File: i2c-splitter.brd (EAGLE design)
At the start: 23.5 x 23.5 mm, 5 parts

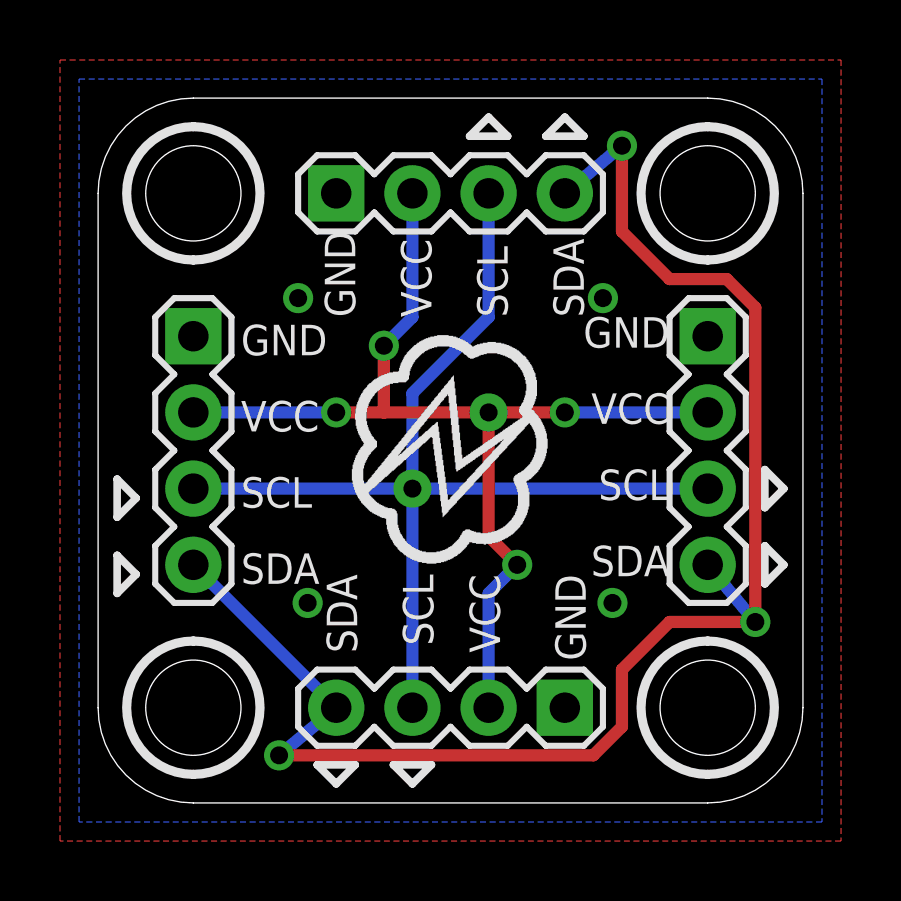
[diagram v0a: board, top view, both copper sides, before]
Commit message: reversed headers
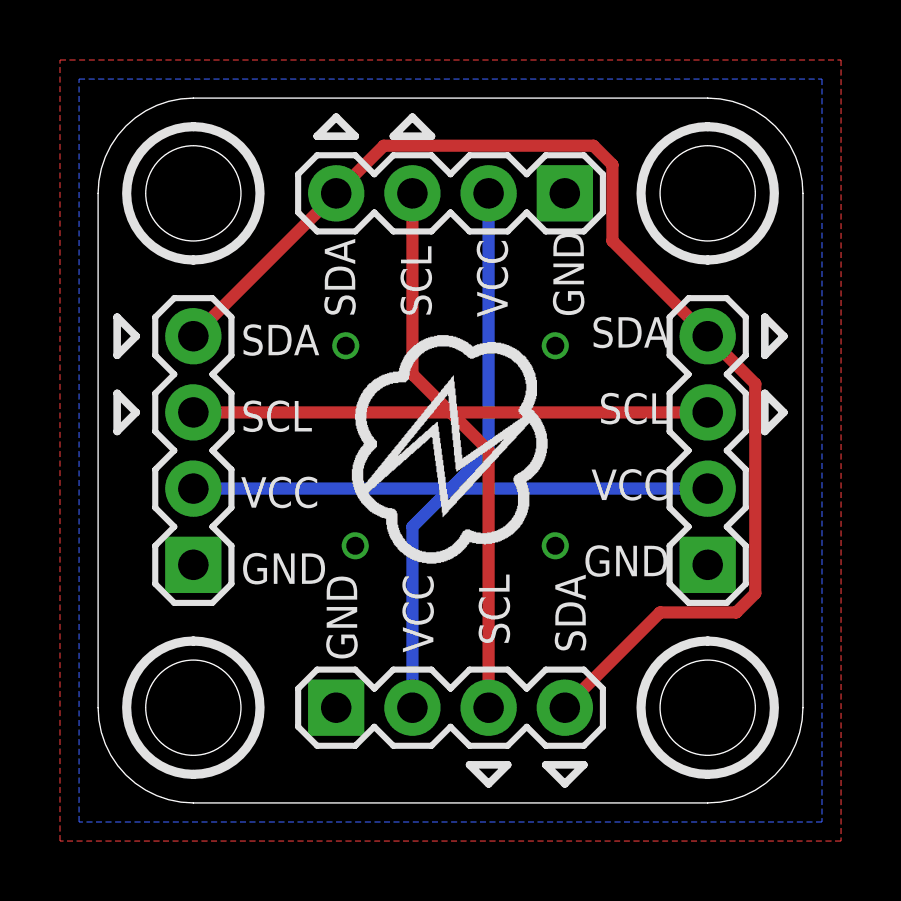
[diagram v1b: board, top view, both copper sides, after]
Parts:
- moved JP1 7.62 mm to (3.17, 7.94), turned to 90 degrees
- moved JP2 7.62 mm to (15.6, 20.3), turned to 180 degrees
- moved JP3 7.62 mm to (20.3, 7.94), turned to 90 degrees
- moved JP4 7.62 mm to (7.94, 3.17), turned to 0 degrees
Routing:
- net SDA: track 51.8 -> 41.1 mm, vias 3 -> 0
- net VCC: track 35.5 -> 35.3 mm, vias 5 -> 0
- net SCL: vias 1 -> 0
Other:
- board text added: "I2C Splitter IX01"
- board text removed: "I2C Splitter IS01"

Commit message: optional bypass capacitor
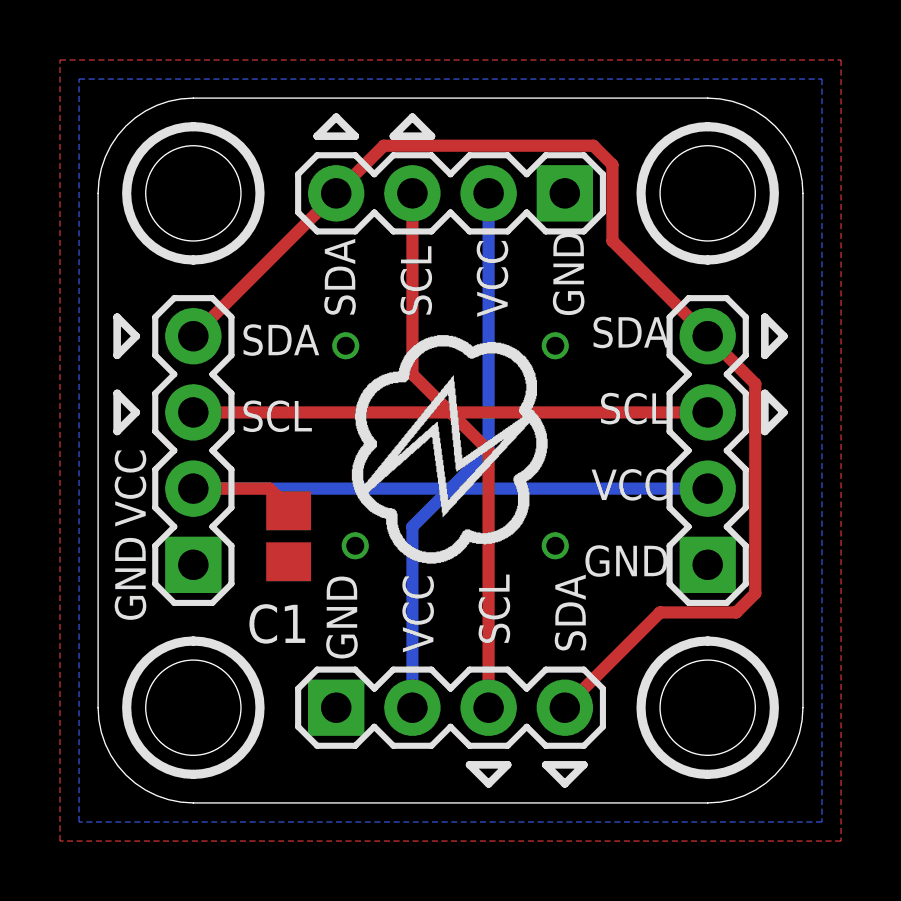
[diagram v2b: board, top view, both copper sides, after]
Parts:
- added C1: 100 nF, resistor:C0805
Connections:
- net GND: now also C1.2
- net VCC: now also C1.1
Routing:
- net VCC: track 35.3 -> 39.0 mm
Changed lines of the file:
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@@
 <layer number="20" name="Dimension" color="15" fill="1" visible="yes" active="yes"/>
 <layer number="21" name="tPlace" color="14" fill="1" visible="yes" active="yes"/>
-<layer number="22" name="bPlace" color="13" fill="1" visible="no" active="yes"/>
+<layer number="22" name="bPlace" color="13" fill="1" visible="yes" active="yes"/>
 <layer number="23" name="tOrigins" color="15" fill="1" visible="yes" active="yes"/>
 <layer number="24" name="bOrigins" color="15" fill="1" visible="yes" active="yes"/>
@@
 <text x="4.7625" y="14.9225" size="1.016" layer="21" font="vector">SDA</text>
 <text x="4.7625" y="12.3825" size="1.016" layer="21" font="vector">SCL</text>
-<text x="4.7625" y="9.8425" size="1.016" layer="21" font="vector">VCC</text>
-<text x="4.7625" y="7.3025" size="1.016" layer="21" font="vector">GND</text>
+<text x="1.5875" y="9.2075" size="1.016" layer="21" font="vector" rot="R90">VCC</text>
+<text x="1.5875" y="6.0325" size="1.016" layer="21" font="vector" rot="R90">GND</text>
 <text x="15.24" y="7.62" size="1.016" layer="21" font="vector" rot="R270">SDA</text>
 <text x="8.5725" y="16.1925" size="1.016" layer="21" font="vector" rot="R90">SDA</text>
@@
 <wire x1="1.27" y1="15.5575" x2="0.635" y2="16.1925" width="0.3048" layer="22"/>
 <wire x1="1.27" y1="15.5575" x2="0.635" y2="14.9225" width="0.3048" layer="22"/>
-<wire x1="7.3025" y1="1.27" x2="8.5725" y2="1.27" width="0.3048" layer="22"/>
-<wire x1="8.5725" y1="1.27" x2="7.9375" y2="0.635" width="0.3048" layer="22"/>
-<wire x1="7.3025" y1="1.27" x2="7.9375" y2="0.635" width="0.3048" layer="22"/>
-<wire x1="10.4775" y1="0.635" x2="9.8425" y2="1.27" width="0.3048" layer="22"/>
-<wire x1="11.1125" y1="1.27" x2="9.8425" y2="1.27" width="0.3048" layer="22"/>
-<wire x1="11.1125" y1="1.27" x2="10.4775" y2="0.635" width="0.3048" layer="22"/>
-<wire x1="22.225" y1="7.3025" x2="22.86" y2="7.9375" width="0.3048" layer="22"/>
-<wire x1="22.86" y1="7.9375" x2="22.225" y2="8.5725" width="0.3048" layer="22"/>
-<wire x1="22.225" y1="8.5725" x2="22.225" y2="7.3025" width="0.3048" layer="22"/>
-<wire x1="22.225" y1="9.8425" x2="22.86" y2="10.4775" width="0.3048" layer="22"/>
-<wire x1="22.86" y1="10.4775" x2="22.225" y2="11.1125" width="0.3048" layer="22"/>
-<wire x1="22.225" y1="11.1125" x2="22.225" y2="9.8425" width="0.3048" layer="22"/>
+<wire x1="12.3825" y1="1.27" x2="13.6525" y2="1.27" width="0.3048" layer="22"/>
+<wire x1="13.6525" y1="1.27" x2="13.0175" y2="0.635" width="0.3048" layer="22"/>
+<wire x1="12.3825" y1="1.27" x2="13.0175" y2="0.635" width="0.3048" layer="22"/>
+<wire x1="15.5575" y1="0.635" x2="14.9225" y2="1.27" width="0.3048" layer="22"/>
+<wire x1="16.1925" y1="1.27" x2="14.9225" y2="1.27" width="0.3048" layer="22"/>
+<wire x1="16.1925" y1="1.27" x2="15.5575" y2="0.635" width="0.3048" layer="22"/>
+<wire x1="22.225" y1="12.3825" x2="22.86" y2="13.0175" width="0.3048" layer="22"/>
+<wire x1="22.86" y1="13.0175" x2="22.225" y2="13.6525" width="0.3048" layer="22"/>
+<wire x1="22.225" y1="13.6525" x2="22.225" y2="12.3825" width="0.3048" layer="22"/>
+<wire x1="22.225" y1="14.9225" x2="22.86" y2="15.5575" width="0.3048" layer="22"/>
+<wire x1="22.86" y1="15.5575" x2="22.225" y2="16.1925" width="0.3048" layer="22"/>
+<wire x1="22.225" y1="16.1925" x2="22.225" y2="14.9225" width="0.3048" layer="22"/>
 <wire x1="7.3025" y1="22.225" x2="7.9375" y2="22.86" width="0.3048" layer="22"/>
 <wire x1="7.9375" y1="22.86" x2="8.5725" y2="22.225" width="0.3048" layer="22"/>
@@
 </element>
 <element name="U$1" library="SparkFun" package="OSHW-LOGO-S" value="" x="11.7475" y="6.985" rot="MR0"/>
+<element name="C1" library="resistor" package="C0805" value="100 nF" x="6.35" y="8.89" smashed="yes" rot="R270">
+<attribute name="NAME" x="7.0485" y="6.604" size="1.27" layer="25" font="vector" rot="R180"/>
+</element>
 </elements>
 <signals>
@@
 <via x="15.24" y="15.24" extent="1-16" drill="0.6" shape="square"/>
 <via x="8.255" y="15.24" extent="1-16" drill="0.6" shape="square"/>
+<contactref element="C1" pad="2"/>
 </signal>
 <signal name="VCC">
@@
 <wire x1="10.4775" y1="3.175" x2="10.4775" y2="9.2075" width="0.4064" layer="16"/>
 <wire x1="13.0175" y1="20.32" x2="13.0175" y2="11.7475" width="0.4064" layer="16"/>
-<wire x1="10.4775" y1="9.2075" x2="11.27125" y2="10.00125" width="0.4064" layer="16"/>
-<wire x1="11.27125" y1="10.00125" x2="11.7475" y2="10.4775" width="0.4064" layer="16"/>
+<wire x1="10.4775" y1="9.2075" x2="11.7475" y2="10.4775" width="0.4064" layer="16"/>
 <wire x1="13.0175" y1="11.7475" x2="11.7475" y2="10.4775" width="0.4064" layer="16"/>
+<contactref element="C1" pad="1"/>
+<wire x1="6.35" y1="9.74" x2="6.4525" y2="9.74" width="0.4064" layer="1"/>
+<wire x1="6.4525" y1="9.74" x2="5.715" y2="10.4775" width="0.4064" layer="1"/>
+<wire x1="5.715" y1="10.4775" x2="3.175" y2="10.4775" width="0.4064" layer="1"/>
 </signal>
 <signal name="SCL">
